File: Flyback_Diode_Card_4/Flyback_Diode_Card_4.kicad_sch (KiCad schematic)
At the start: 12 parts, among them J1 Screw_Terminal_01x06, J2 Screw_Terminal_01x06, J3 Screw_Terminal_01x02, J4 Screw_Terminal_01x12, J5 Screw_Terminal_01x12, J6 Screw_Terminal_01x04, J7 Screw_Terminal_01x02, J8 Screw_Terminal_01x02

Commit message: Working on new flyback diode card/
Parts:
- J7, J8: footprint TerminalBlock_Phoenix:TerminalBlock_Phoenix_MKDS-3-2-5.08_1x02_P5.08mm_Horizontal -> Connector_Phoenix_MC_HighVoltage:PhoenixContact_MCV_1,5_2-G-5.08_1x02_P5.08mm_Vertical
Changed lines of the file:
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@@
 			)
 		)
-		(property "Footprint" "TerminalBlock_Phoenix:TerminalBlock_Phoenix_MKDS-3-2-5.08_1x02_P5.08mm_Horizontal"
+		(property "Footprint" "Connector_Phoenix_MC_HighVoltage:PhoenixContact_MCV_1,5_2-G-5.08_1x02_P5.08mm_Vertical"
 			(at 41.91 156.21 0)
 			(effects
@@
 			)
 		)
-		(property "Footprint" "TerminalBlock_Phoenix:TerminalBlock_Phoenix_MKDS-3-2-5.08_1x02_P5.08mm_Horizontal"
+		(property "Footprint" "Connector_Phoenix_MC_HighVoltage:PhoenixContact_MCV_1,5_2-G-5.08_1x02_P5.08mm_Vertical"
 			(at 255.27 156.21 0)
 			(effects

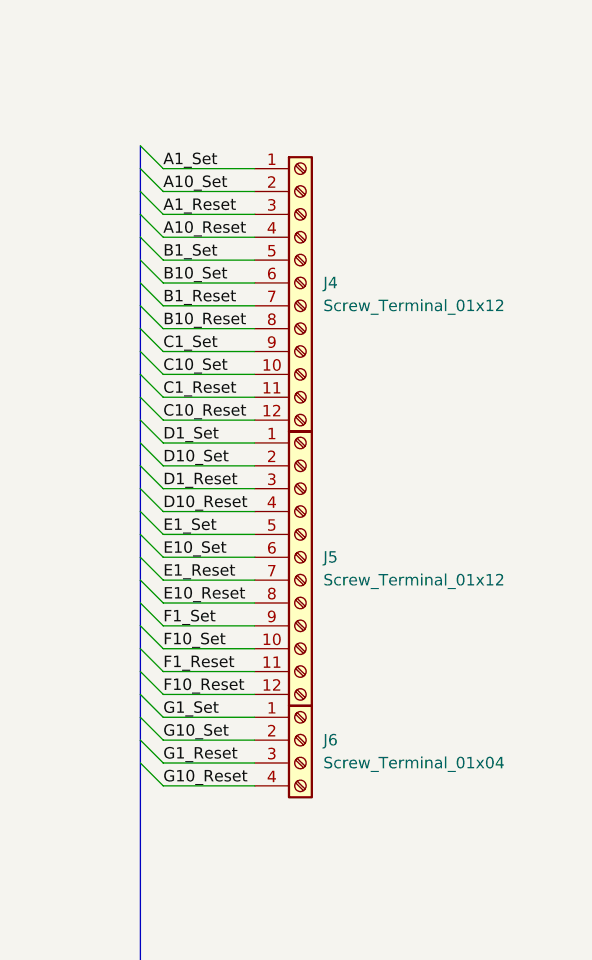
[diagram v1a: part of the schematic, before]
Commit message: Finished and submitted for manufacturing  New PCB Flyback Board
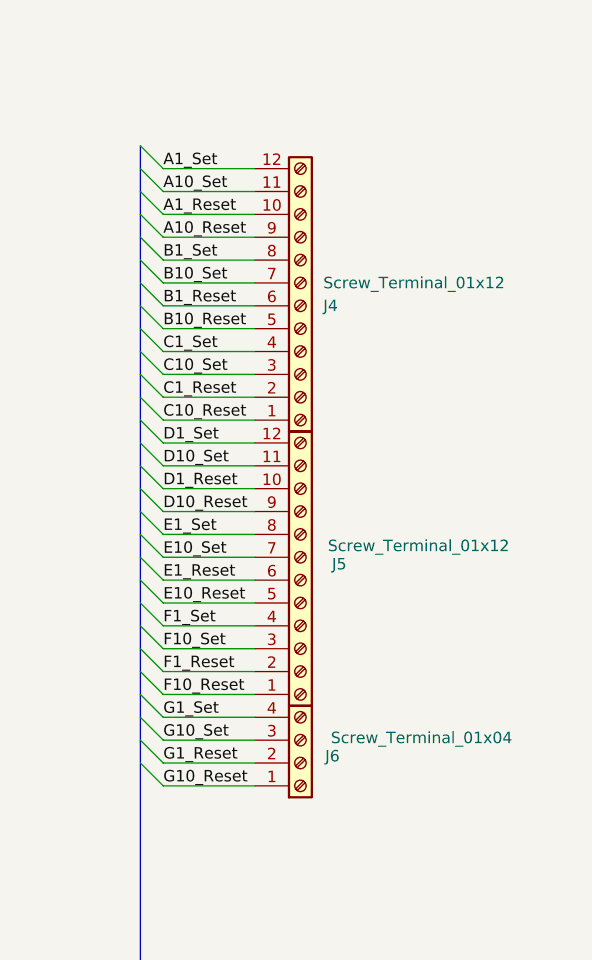
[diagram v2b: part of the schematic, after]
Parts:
- J1, J2: footprint Connector_Phoenix_MC_HighVoltage:PhoenixContact_MCV_1,5_6-G-5.08_1x06_P5.08mm_Vertical -> TerminalBlock_Phoenix:TerminalBlock_Phoenix_MKDS-1,5-6-5.08_1x06_P5.08mm_Horizontal
- J3, J7, J8: footprint Connector_Phoenix_MC_HighVoltage:PhoenixContact_MCV_1,5_2-G-5.08_1x02_P5.08mm_Vertical -> TerminalBlock_Phoenix:TerminalBlock_Phoenix_MKDS-1,5-2-5.08_1x02_P5.08mm_Horizontal
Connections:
- net A10_Reset: now also J4.9 (Pin_9); no longer J4.4 (Pin_4)
- net A10_Set: now also J4.11 (Pin_11); no longer J4.2 (Pin_2)
- net A1_Reset: now also J4.10 (Pin_10); no longer J4.3 (Pin_3)
- net A1_Set: now also J4.12 (Pin_12); no longer J4.1 (Pin_1)
- net B10_Reset: now also J4.5 (Pin_5); no longer J4.8 (Pin_8)
- net B10_Set: now also J4.7 (Pin_7); no longer J4.6 (Pin_6)
- net B1_Reset: now also J4.6 (Pin_6); no longer J4.7 (Pin_7)
- net B1_Set: now also J4.8 (Pin_8); no longer J4.5 (Pin_5)
- net C10_Reset: now also J4.1 (Pin_1); no longer J4.12 (Pin_12)
- net C10_Set: now also J4.3 (Pin_3); no longer J4.10 (Pin_10)
- net C1_Reset: now also J4.2 (Pin_2); no longer J4.11 (Pin_11)
- net C1_Set: now also J4.4 (Pin_4); no longer J4.9 (Pin_9)
- net D10_Reset: now also J5.9 (Pin_9); no longer J5.4 (Pin_4)
- net D10_Set: now also J5.11 (Pin_11); no longer J5.2 (Pin_2)
- net D1_Reset: now also J5.10 (Pin_10); no longer J5.3 (Pin_3)
- net D1_Set: now also J5.12 (Pin_12); no longer J5.1 (Pin_1)
- net E10_Reset: now also J5.5 (Pin_5); no longer J5.8 (Pin_8)
- net E10_Set: now also J5.7 (Pin_7); no longer J5.6 (Pin_6)
- net E1_Reset: now also J5.6 (Pin_6); no longer J5.7 (Pin_7)
- net E1_Set: now also J5.8 (Pin_8); no longer J5.5 (Pin_5)
- net F10_Reset: now also J5.1 (Pin_1); no longer J5.12 (Pin_12)
- net F10_Set: now also J5.3 (Pin_3); no longer J5.10 (Pin_10)
- net F1_Reset: now also J5.2 (Pin_2); no longer J5.11 (Pin_11)
- net F1_Set: now also J5.4 (Pin_4); no longer J5.9 (Pin_9)
- net G10_Reset: now also J6.1 (Pin_1); no longer J6.4 (Pin_4)
- net G10_Set: now also J6.3 (Pin_3); no longer J6.2 (Pin_2)
- net G1_Reset: now also J6.2 (Pin_2); no longer J6.3 (Pin_3)
- net G1_Set: now also J6.4 (Pin_4); no longer J6.1 (Pin_1)
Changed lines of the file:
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@@
 			)
 		)
-		(property "Footprint" "Connector_Phoenix_MC_HighVoltage:PhoenixContact_MCV_1,5_6-G-5.08_1x06_P5.08mm_Vertical"
+		(property "Footprint" "TerminalBlock_Phoenix:TerminalBlock_Phoenix_MKDS-1,5-6-5.08_1x06_P5.08mm_Horizontal"
 			(at 38.1 35.56 0)
 			(effects
@@
 			)
 		)
-		(property "Footprint" "Connector_Phoenix_MC_HighVoltage:PhoenixContact_MCV_1,5_2-G-5.08_1x02_P5.08mm_Vertical"
+		(property "Footprint" "TerminalBlock_Phoenix:TerminalBlock_Phoenix_MKDS-1,5-2-5.08_1x02_P5.08mm_Horizontal"
 			(at 41.91 156.21 0)
 			(effects
@@
 	(symbol
 		(lib_id "Connector:Screw_Terminal_01x04")
-		(at 252.73 93.98 0)
-		(unit 1)
-		(exclude_from_sim no)
-		(in_bom yes)
-		(on_board yes)
-		(dnp no)
-		(fields_autoplaced yes)
+		(at 252.73 96.52 0)
+		(mirror x)
+		(unit 1)
+		(exclude_from_sim no)
+		(in_bom yes)
+		(on_board yes)
+		(dnp no)
 		(property "Reference" "J6"
-			(at 255.27 93.98 0)
-			(effects
-				(font
-					(size 1.27 1.27)
-				)
-				(justify left)
+			(at 256.286 95.758 0)
+			(effects
+				(font
+					(size 1.27 1.27)
+				)
 			)
 		)
 		(property "Value" "Screw_Terminal_01x04"
-			(at 255.27 96.52 0)
-			(effects
-				(font
-					(size 1.27 1.27)
-				)
-				(justify left)
+			(at 266.192 93.726 0)
+			(effects
+				(font
+					(size 1.27 1.27)
+				)
 			)
 		)
 		(property "Footprint" "TerminalBlock_Phoenix:TerminalBlock_Phoenix_MPT-0,5-4-2.54_1x04_P2.54mm_Horizontal"
-			(at 252.73 93.98 0)
-			(effects
-				(font
-					(size 1.27 1.27)
-				)
-				(hide yes)
-			)
-		)
-		(property "Datasheet" "~"
-			(at 252.73 93.98 0)
-			(effects
-				(font
-					(size 1.27 1.27)
-				)
-				(hide yes)
-			)
-		)
-		(property "Description" ""
-			(at 252.73 93.98 0)
+			(at 252.73 96.52 0)
+			(effects
+				(font
+					(size 1.27 1.27)
+				)
+				(hide yes)
+			)
+		)
+		(property "Datasheet" "~"
+			(at 252.73 96.52 0)
+			(effects
+				(font
+					(size 1.27 1.27)
+				)
+				(hide yes)
+			)
+		)
+		(property "Description" ""
+			(at 252.73 96.52 0)
 			(effects
 				(font
@@
 	(symbol
 		(lib_id "Connector:Screw_Terminal_01x12")
-		(at 252.73 73.66 0)
-		(unit 1)
-		(exclude_from_sim no)
-		(in_bom yes)
-		(on_board yes)
-		(dnp no)
-		(fields_autoplaced yes)
+		(at 252.73 76.2 0)
+		(mirror x)
+		(unit 1)
+		(exclude_from_sim no)
+		(in_bom yes)
+		(on_board yes)
+		(dnp no)
 		(property "Reference" "J5"
-			(at 255.27 73.66 0)
-			(effects
-				(font
-					(size 1.27 1.27)
-				)
-				(justify left)
+			(at 257.048 74.422 0)
+			(effects
+				(font
+					(size 1.27 1.27)
+				)
 			)
 		)
 		(property "Value" "Screw_Terminal_01x12"
-			(at 255.27 76.2 0)
+			(at 255.778 72.39 0)
 			(effects
 				(font
@@
 		)
 		(property "Footprint" "TerminalBlock_Phoenix:TerminalBlock_Phoenix_MPT-0,5-12-2.54_1x12_P2.54mm_Horizontal"
-			(at 252.73 73.66 0)
-			(effects
-				(font
-					(size 1.27 1.27)
-				)
-				(hide yes)
-			)
-		)
-		(property "Datasheet" "~"
-			(at 252.73 73.66 0)
-			(effects
-				(font
-					(size 1.27 1.27)
-				)
-				(hide yes)
-			)
-		)
-		(property "Description" ""
-			(at 252.73 73.66 0)
+			(at 252.73 76.2 0)
+			(effects
+				(font
+					(size 1.27 1.27)
+				)
+				(hide yes)
+			)
+		)
+		(property "Datasheet" "~"
+			(at 252.73 76.2 0)
+			(effects
+				(font
+					(size 1.27 1.27)
+				)
+				(hide yes)
+			)
+		)
+		(property "Description" ""
+			(at 252.73 76.2 0)
 			(effects
 				(font
@@
 	(symbol
 		(lib_id "Connector:Screw_Terminal_01x12")
-		(at 252.73 43.18 0)
-		(unit 1)
-		(exclude_from_sim no)
-		(in_bom yes)
-		(on_board yes)
-		(dnp no)
-		(fields_autoplaced yes)
+		(at 252.73 45.72 0)
+		(mirror x)
+		(unit 1)
+		(exclude_from_sim no)
+		(in_bom yes)
+		(on_board yes)
+		(dnp no)
 		(property "Reference" "J4"
+			(at 255.27 45.72 0)
+			(effects
+				(font
+					(size 1.27 1.27)
+				)
+				(justify left)
+			)
+		)
+		(property "Value" "Screw_Terminal_01x12"
 			(at 255.27 43.18 0)
 			(effects
@@
 			)
 		)
-		(property "Value" "Screw_Terminal_01x12"
-			(at 255.27 45.72 0)
-			(effects
-				(font
-					(size 1.27 1.27)
-				)
-				(justify left)
-			)
-		)
 		(property "Footprint" "TerminalBlock_Phoenix:TerminalBlock_Phoenix_MPT-0,5-12-2.54_1x12_P2.54mm_Horizontal"
-			(at 252.73 43.18 0)
-			(effects
-				(font
-					(size 1.27 1.27)
-				)
-				(hide yes)
-			)
-		)
-		(property "Datasheet" "~"
-			(at 252.73 43.18 0)
-			(effects
-				(font
-					(size 1.27 1.27)
-				)
-				(hide yes)
-			)
-		)
-		(property "Description" ""
-			(at 252.73 43.18 0)
+			(at 252.73 45.72 0)
+			(effects
+				(font
+					(size 1.27 1.27)
+				)
+				(hide yes)
+			)
+		)
+		(property "Datasheet" "~"
+			(at 252.73 45.72 0)
+			(effects
+				(font
+					(size 1.27 1.27)
+				)
+				(hide yes)
+			)
+		)
+		(property "Description" ""
+			(at 252.73 45.72 0)
 			(effects
 				(font
@@
 			)
 		)
-		(property "Footprint" "Connector_Phoenix_MC_HighVoltage:PhoenixContact_MCV_1,5_2-G-5.08_1x02_P5.08mm_Vertical"
+		(property "Footprint" "TerminalBlock_Phoenix:TerminalBlock_Phoenix_MKDS-1,5-2-5.08_1x02_P5.08mm_Horizontal"
 			(at 255.27 156.21 0)
 			(effects
@@
 			)
 		)
-		(property "Footprint" "Connector_Phoenix_MC_HighVoltage:PhoenixContact_MCV_1,5_2-G-5.08_1x02_P5.08mm_Vertical"
+		(property "Footprint" "TerminalBlock_Phoenix:TerminalBlock_Phoenix_MKDS-1,5-2-5.08_1x02_P5.08mm_Horizontal"
 			(at 38.1 60.96 0)
 			(effects
@@
 			)
 		)
-		(property "Footprint" "Connector_Phoenix_MC_HighVoltage:PhoenixContact_MCV_1,5_6-G-5.08_1x06_P5.08mm_Vertical"
+		(property "Footprint" "TerminalBlock_Phoenix:TerminalBlock_Phoenix_MKDS-1,5-6-5.08_1x06_P5.08mm_Horizontal"
 			(at 38.1 50.8 0)
 			(effects
